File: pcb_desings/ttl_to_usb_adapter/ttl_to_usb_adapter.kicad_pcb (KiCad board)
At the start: 2 copper layers, 16 x 19 mm, 10 parts, among them J1 CH_PD_selector, Q1 UMH3N, U1 USB_to_TTL, U2 TTL_to_USB_adapter_iot_postbox

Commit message: Updated iot-postbox pcb to v0.0
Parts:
- U2: value TTL_to_USB_adapter_iot_postbox -> TTL_UART_adapter_iot_postbox; footprint ttl_to_usb_adapter:TTL_to_USB_PinHeader -> Connector_PinHeader_2.54mm:PinHeader_1x07_P2.54mm_Vertical
- moved U2 2.41 mm to (168.2, 103.2), turned to 180 degrees

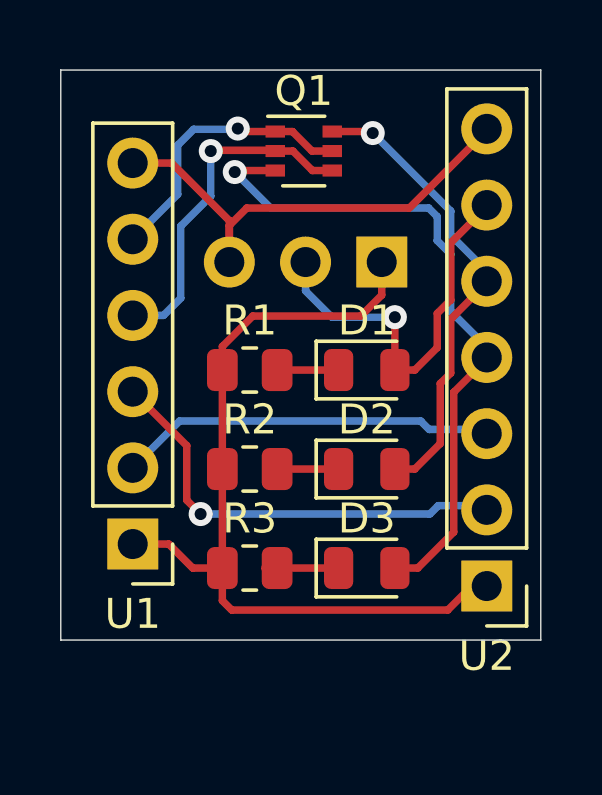
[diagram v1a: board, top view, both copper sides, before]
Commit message: Added ttl_to_usb_adapter board and exported pcbs panelized
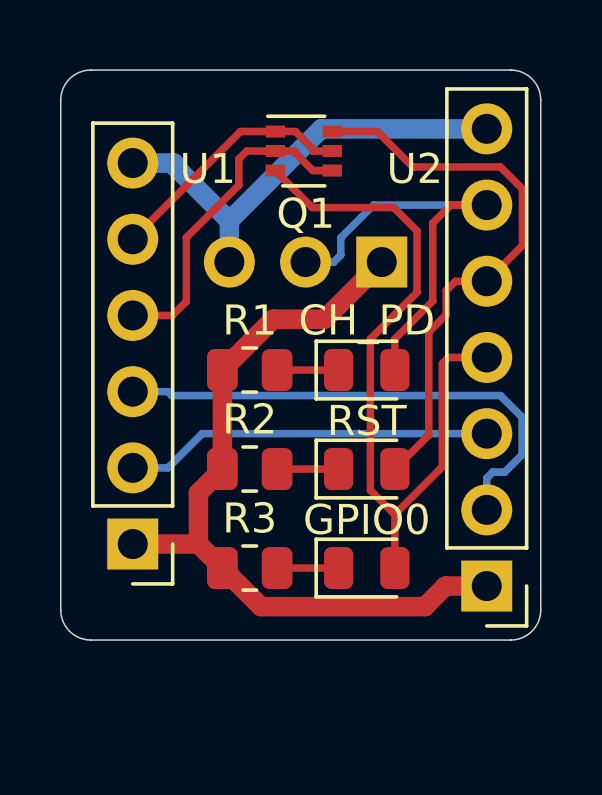
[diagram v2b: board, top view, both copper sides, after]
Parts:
- renumbered D1 to CH_PD, D3 to GPIO0, D2 to RST
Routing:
- net /RST: track 16.0 -> 18.8 mm, vias 1 -> 0
- net /GPIO0: track 23.0 -> 25.7 mm, vias 1 -> 0
- net /GND: track 28.4 -> 25.9 mm
- net /TXD: track 15.6 -> 17.1 mm, vias 1 -> 0
- net /3V3: track 16.8 -> 15.3 mm
- net /CH_PD: track 13.4 -> 14.6 mm, vias 1 -> 0
- net /RTS: track 9.45 -> 8.45 mm, vias 1 -> 0
- net /DTR: track 11.5 -> 11.0 mm, vias 1 -> 0
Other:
- outline, holes or cut-outs redrawn
- net class POWER added: clearance 0.2, trace_width 0.65, via_dia 0.8, via_drill 0.4
- board text added: "3V3"
- board text added: "CH_PD"
- board text added: "DTR"
- board text added: "GND"
- board text added: "GPIO0"
- board text added: "RST"
- board text added: "RTS"
- board text added: "RX"
- board text added: "RXD"
- board text added: "TTL to USB adapter"
- board text added: "TX"
- board text added: "TXD"
- board text added: "v0.0"
